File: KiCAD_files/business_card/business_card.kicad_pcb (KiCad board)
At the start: 2 copper layers, 89 x 50.8 mm, 82 parts, among them J1 USB_C_Receptacle_USB2.0_14P, J2 Conn_01x05_Pin, SW1 SW_MEC_5E, SW2 SW_MEC_5E, SW3 SW_MEC_5E, SW4 SW_MEC_5E, SW5 SW_MEC_5E, SW6 SW_MEC_5E, SW7 SW_MEC_5E, SW8 SW_Push, U1 STM32U073CCUx, U2 MCP1700x-300xxTT, U3 TPS3839DBZ

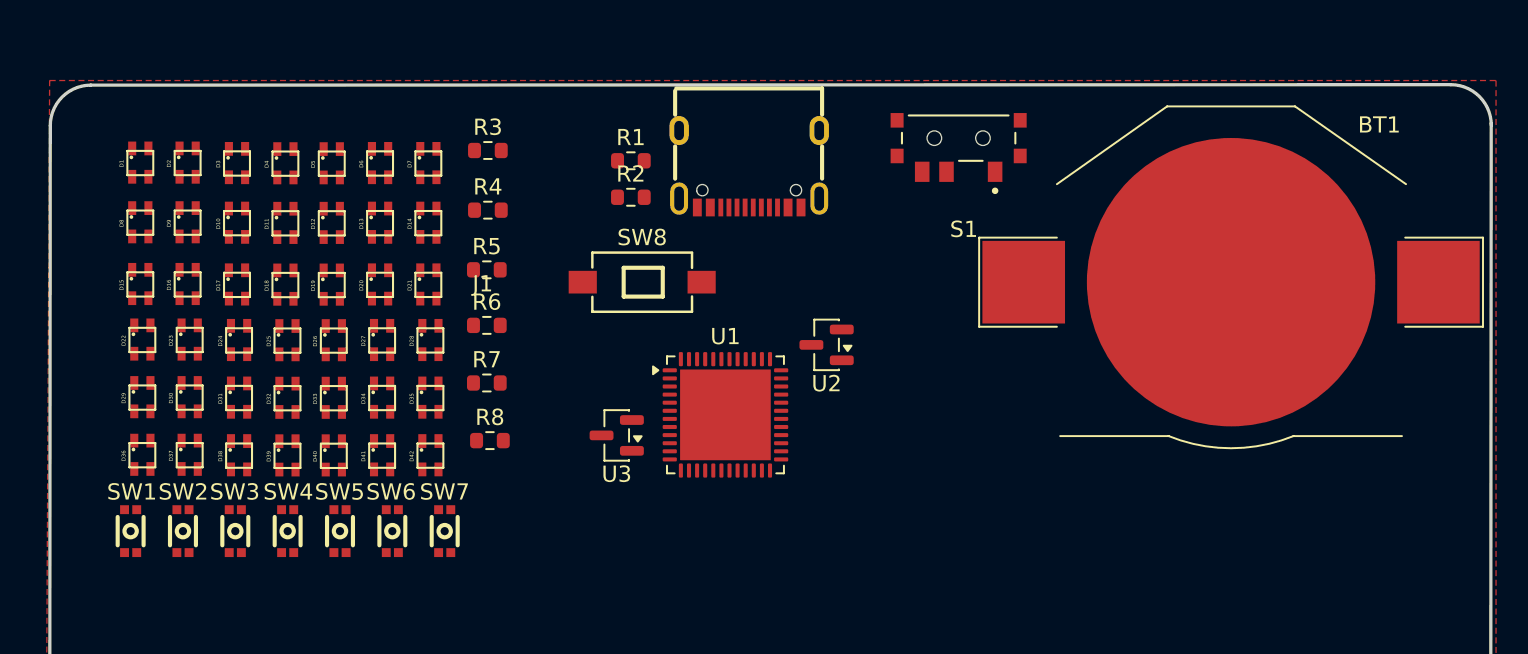
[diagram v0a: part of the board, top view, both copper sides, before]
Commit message: Change Connections to Match STM32C0 Spec
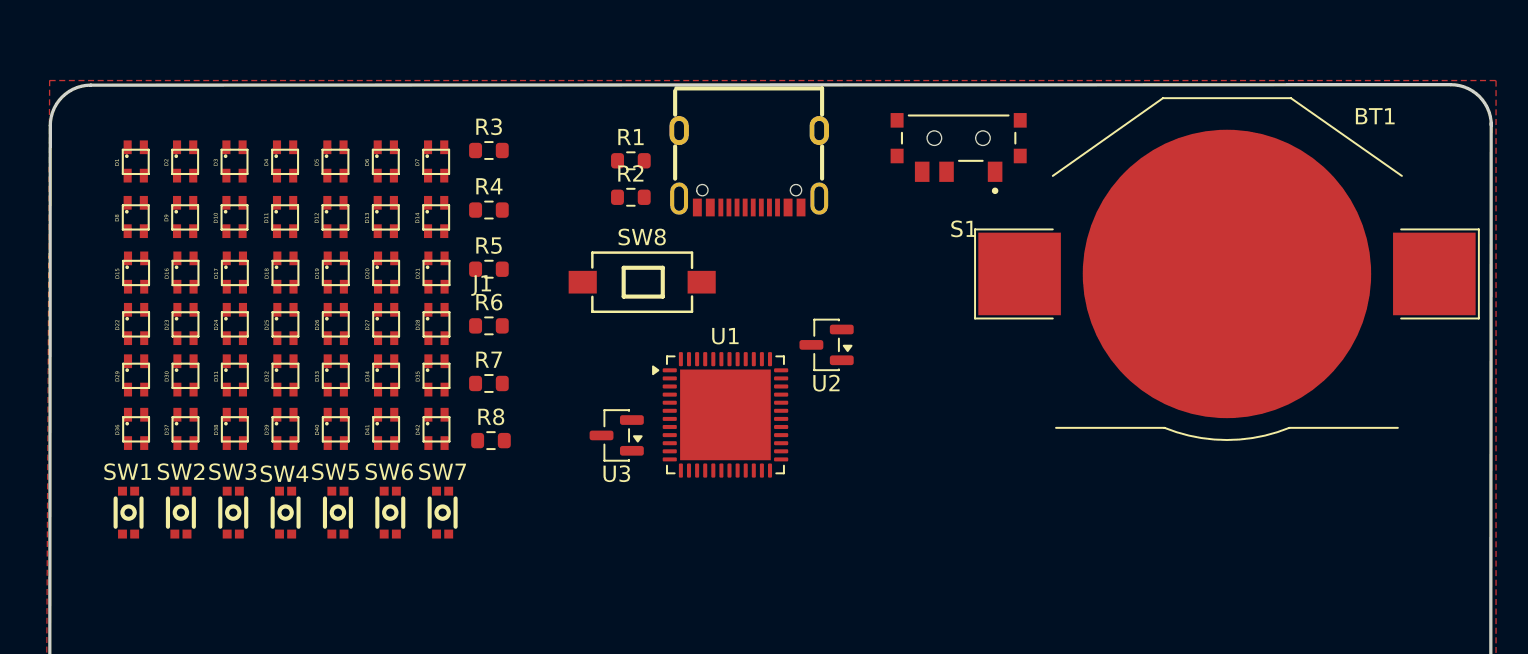
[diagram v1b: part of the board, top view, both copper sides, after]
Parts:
- moved D42 1.67 mm to (113.8, 68.8)
- moved D38 1.64 mm to (101.3, 68.8)
- moved D41 1.64 mm to (110.7, 68.8)
- moved D36 1.64 mm to (95.3, 68.8)
- moved D39 1.64 mm to (104.5, 68.8)
- moved D40 1.64 mm to (107.6, 68.8)
- moved D37 1.62 mm to (98.3, 68.8)
- moved D35 1.42 mm to (113.8, 65.5)
- moved D29 1.40 mm to (95.3, 65.5)
- moved D31 1.39 mm to (101.3, 65.5)
- moved D34 1.39 mm to (110.7, 65.5)
- moved D32 1.39 mm to (104.5, 65.5)
- moved D33 1.39 mm to (107.6, 65.5)
- moved D30 1.37 mm to (98.3, 65.5)
- moved SW2 1.15 mm to (98.0, 74.0)
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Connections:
- S1 pad 1: /VDDUSB -> Net-(BT1-+)
- S1 pad 3: Net-(BT1-+) -> /VDDUSB

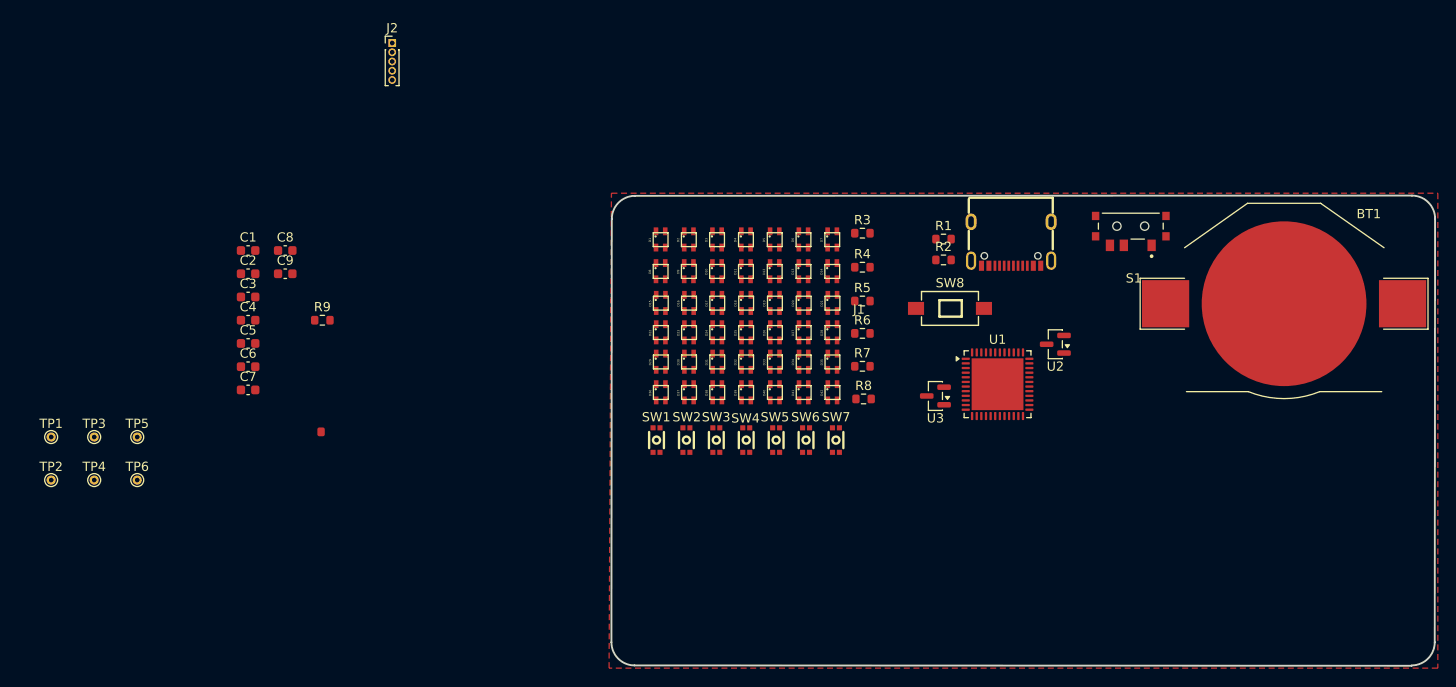
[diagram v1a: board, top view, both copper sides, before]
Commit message: Switch Button types, Add 3D Models to Components
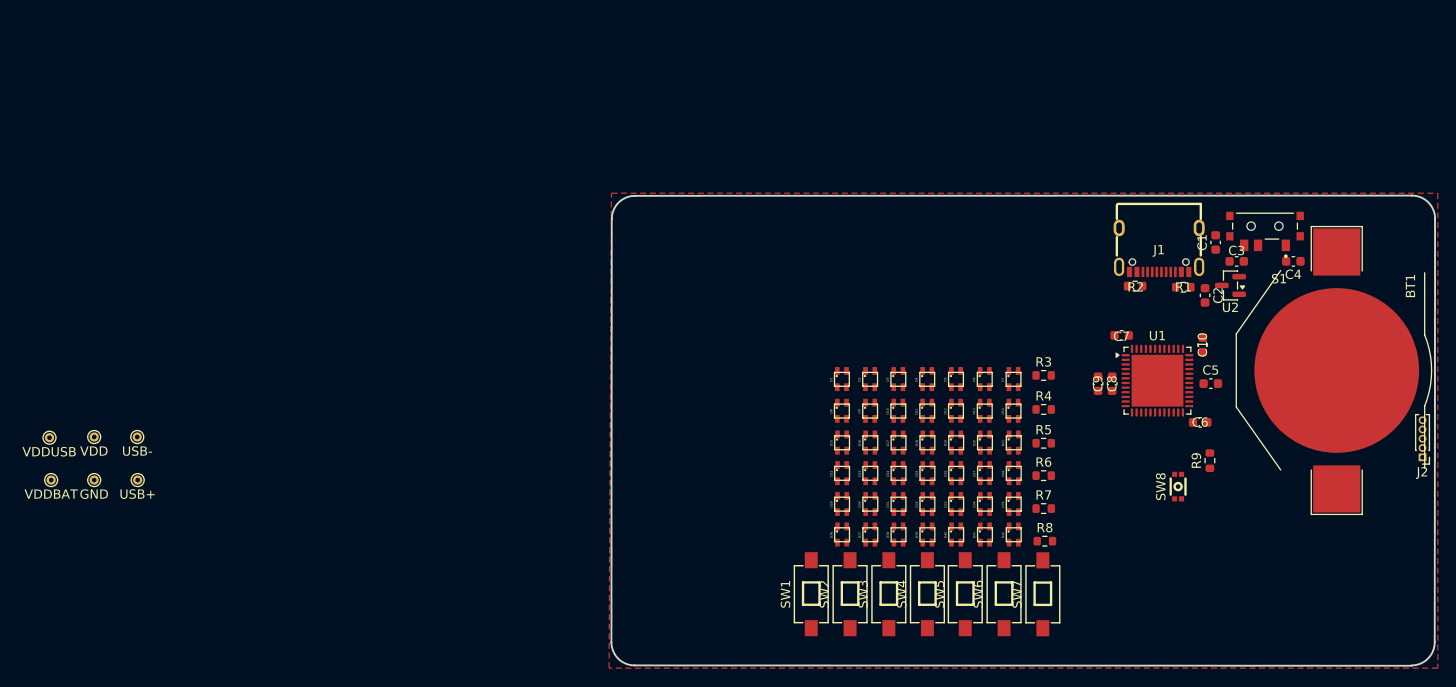
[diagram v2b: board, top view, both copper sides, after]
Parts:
- removed ?: , 
- removed the C4 at (50.7, 61.1)
- removed U3: TPS3839DBZ, Package_TO_SOT_SMD:SOT-23
- added C1: 4.7uF, Capacitor_SMD:C_0603_1608Metric, F.Cu at (155.2, 52.7)
- added C10: 4.7uF, Capacitor_SMD:C_0603_1608Metric, F.Cu at (153.8, 63.8)
- C8: value 1uF -> 10nF
- SW1, SW2, SW3, SW4, SW5, SW6, SW7: value SW_MEC_5E -> SW_Push; footprint 1TS026A-2000-0553-CT:SW-SMD_4P-L2.6-W1.6-P0.75-LS3.0 -> TSB008A2526A:TSB008A2526A
- SW8: value SW_Push -> SW_MEC_5E; footprint TSB008A2526A:TSB008A2526A -> 1TS026A-2000-0553-CT:SW-SMD_4P-L2.6-W1.6-P0.75-LS3.0
- moved J2 120.0 mm to (177.5, 75.9), turned to 180 degrees
- moved C4 108.9 mm to (163.6, 54.7), turned to 180 degrees
- moved C3 107.7 mm to (157.5, 54.7), turned to 180 degrees
- moved C5 105.0 mm to (154.7, 67.9)
- moved C6 104.1 mm to (153.5, 72.1)
- moved C2 103.7 mm to (154.1, 58.4), turned to -90 degrees
- moved R9 97.1 mm to (154.6, 76.3), turned to 90 degrees
- moved C7 94.5 mm to (145.0, 62.7), turned to 180 degrees
- moved C9 91.9 mm to (142.5, 68.0), turned to 90 degrees
- moved C8 90.5 mm to (144.0, 68.0), turned to 90 degrees
- moved SW8 31.3 mm to (151.1, 79.1), turned to 90 degrees
- moved SW7 27.9 mm to (136.5, 90.7)
- moved SW6 27.1 mm to (132.3, 90.7)
- moved R1 26.4 mm to (151.7, 57.5), turned to 180 degrees
- moved SW5 26.4 mm to (128.1, 90.7)
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- renumbered C6 to C2, C7 to C3, C9 to C4, C1 to C5, C2 to C6, C3 to C7, C5 to C9
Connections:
- C5 pad 1: +3.3V -> VDD
- C6 pad 1: +3.3V -> VDD
- C7 pad 1: +3.3V -> VDD
- C8 pad 1: GND -> VDD
- C8 pad 2: +3.3V -> GND
- C9 pad 1: +3.3V -> VDD
- J1 pad 1: (no net) -> GND
- J1 pad 10: (no net) -> Net-(J1-CC2)
- J1 pad 11: (no net) -> Net-(U2-VI)
- J1 pad 12: (no net) -> GND
- J1 pad 13: (no net) -> GND
- J1 pad 14: (no net) -> GND
- J1 pad 2: (no net) -> Net-(U2-VI)
- J1 pad 3: (no net) -> unconnected-(J1-SBU2-Pad3)
- J1 pad 4: (no net) -> Net-(J1-CC1)
- J1 pad 5: (no net) -> /USB-
- J1 pad 6: (no net) -> /USB+
- J1 pad 7: (no net) -> /USB-
- J1 pad 8: (no net) -> /USB+
- J1 pad 9: (no net) -> unconnected-(J1-SBU1-Pad9)
- J2 pad 1: +3.3V -> VDD
- R9 pad 1: Net-(U1-PF3) -> Net-(SW8-A)
- S1 pad 2: +3.3V -> VDD
- SW1 pad 2: unconnected-(SW1-Pad2) -> VDD
- SW2 pad 2: unconnected-(SW2-Pad2) -> VDD
- SW3 pad 2: unconnected-(SW3-Pad2) -> VDD
- SW4 pad 2: unconnected-(SW4-Pad2) -> VDD
- SW5 pad 2: unconnected-(SW5-Pad2) -> VDD
- SW6 pad 2: unconnected-(SW6-Pad2) -> VDD
- SW7 pad 2: unconnected-(SW7-Pad2) -> VDD
- SW8 pad 1: +3.3V -> VDD
- SW8 pad 2: Net-(U1-PF3) -> unconnected-(SW8-Pad2)
- TP3 pad 1: +3.3V -> VDD
- U1 pad 1: +3.3V -> VDD
- U1 pad 10: unconnected-(U1-PA0-Pad10) -> /VDDUSB
- U1 pad 24: +3.3V -> VDD
- U1 pad 36: /VDDUSB -> VDD
- U1 pad 38: /VDDUSB -> unconnected-(U1-PA15-Pad38)
- U1 pad 44: Net-(U1-PF3) -> Net-(SW8-A)
- U1 pad 48: +3.3V -> VDD
- U1 pad 9: GND -> VDD

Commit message: PCB Layout
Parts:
- removed TP4: GND, TestPoint:TestPoint_THTPad_D1.0mm_Drill0.5mm
- removed TP5: USB-, TestPoint:TestPoint_THTPad_D1.0mm_Drill0.5mm
- removed TP6: USB+, TestPoint:TestPoint_THTPad_D1.0mm_Drill0.5mm
- added C11: 100nF, Capacitor_SMD:C_0603_1608Metric, F.Cu at (150.4, 77.5)
- TP2: value VDDBAT -> GND
- moved TP1 141.7 mm to (170.9, 72.1)
- moved TP2 137.5 mm to (166.9, 75.4)
- moved TP3 137.0 mm to (170.9, 70.1)
- moved J2 42.0 mm to (144.8, 49.5), turned to 90 degrees
- moved J1 40.7 mm to (173.0, 86.4), turned to 90 degrees
- moved R1 35.9 mm to (169.0, 89.0), turned to 90 degrees
- moved R2 34.7 mm to (169.1, 83.8), turned to -90 degrees
- moved C1 32.1 mm to (171.7, 80.3), turned to 180 degrees
- moved C7 27.5 mm to (160.0, 85.9), turned to 0 degrees
- moved C2 26.9 mm to (171.7, 78.7), turned to 180 degrees
- moved U2 26.0 mm to (173.7, 77.0), turned to -90 degrees
- moved S1 24.6 mm to (175.3, 70.6), turned to 90 degrees
- moved C3 24.3 mm to (171.4, 74.6), turned to 90 degrees
- moved D15 17.9 mm to (97.0, 74.9), turned to 180 degrees
- moved D1 17.9 mm to (97.0, 68.0), turned to 180 degrees
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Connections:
- D12 pad 1: Net-(D12-Pad1) -> /COL5
- D12 pad 3: Net-(D12-Pad1) -> /COL5
- D13 pad 1: Net-(D13-Pad1) -> /COL6
- D13 pad 3: Net-(D13-Pad1) -> /COL6
- D19 pad 1: Net-(D12-Pad1) -> /COL5
- D19 pad 3: Net-(D12-Pad1) -> /COL5
- D20 pad 1: Net-(D13-Pad1) -> /COL6
- D20 pad 3: Net-(D13-Pad1) -> /COL6
- D26 pad 1: Net-(D12-Pad1) -> /COL5
- D26 pad 3: Net-(D12-Pad1) -> /COL5
- D27 pad 1: Net-(D13-Pad1) -> /COL6
- D27 pad 3: Net-(D13-Pad1) -> /COL6
- D33 pad 1: Net-(D29-Pad2) -> /COL5
- D33 pad 3: Net-(D29-Pad2) -> /COL5
- D34 pad 1: Net-(D13-Pad1) -> /COL6
- D34 pad 3: Net-(D13-Pad1) -> /COL6
- D36 pad 2: /COL5 -> Net-(D36-Pad2)
- D36 pad 4: /COL5 -> Net-(D36-Pad2)
- D37 pad 2: /COL5 -> Net-(D36-Pad2)
- D37 pad 4: /COL5 -> Net-(D36-Pad2)
- D38 pad 2: /COL5 -> Net-(D36-Pad2)
- D38 pad 4: /COL5 -> Net-(D36-Pad2)
- D39 pad 2: /COL5 -> Net-(D36-Pad2)
- D39 pad 4: /COL5 -> Net-(D36-Pad2)
- D40 pad 2: /COL5 -> Net-(D36-Pad2)
- D40 pad 4: /COL5 -> Net-(D36-Pad2)
- D41 pad 1: /COL5 -> /COL6
- D41 pad 2: /COL5 -> Net-(D36-Pad2)
- D41 pad 3: /COL5 -> /COL6
- D41 pad 4: /COL5 -> Net-(D36-Pad2)
- D42 pad 2: /COL5 -> Net-(D36-Pad2)
- D42 pad 4: /COL5 -> Net-(D36-Pad2)
- D5 pad 1: Net-(D12-Pad1) -> /COL5
- D5 pad 3: Net-(D12-Pad1) -> /COL5
- D6 pad 1: Net-(D13-Pad1) -> /COL6
- D6 pad 3: Net-(D13-Pad1) -> /COL6
- R8 pad 1: /COL5 -> Net-(D36-Pad2)
- S1 pad 1: Net-(BT1-+) -> /VDDUSB
- S1 pad 3: /VDDUSB -> Net-(BT1-+)
- TP2 pad 1: Net-(BT1-+) -> GND
- U1 pad 22: /COL5 -> /COL6
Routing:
- net VDD: track 0.00 -> 25.0 mm
- net /COL4: track 0.00 -> 13.9 mm
- net /COL2: track 0.00 -> 13.7 mm
- net /COL5: track 0.00 -> 13.6 mm
- net /COL1: track 0.00 -> 13.5 mm
- net /COL3: track 0.00 -> 13.4 mm
- net /COL6: track 0.00 -> 13.4 mm
- net /COL7: track 0.00 -> 13.3 mm
- net Net-(BT1-+): track 0.00 -> 10.9 mm
- net /USB+: track 0.00 -> 5.38 mm
- net /VDDUSB: track 0.00 -> 4.87 mm
- net /USB-: track 0.00 -> 4.38 mm, vias 0 -> 2
- net Net-(U2-VI): track 0.00 -> 3.11 mm
- net Net-(J1-CC1): track 0.00 -> 1.87 mm
- net Net-(J1-CC2): track 0.00 -> 1.54 mm

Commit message: Fix Edge Cuts
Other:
- board size 89 x 50.8 mm -> 88.9 x 50.8 mm
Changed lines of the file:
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@@
 				(font
 					(size 0.24 0.24)
+					(thickness 0.15)
 				)
 			)
@@
 		(tags "capacitor")
 		(property "Reference" "C10"
-			(at 0 0 90)
+			(at 0 2.292 180)
 			(layer "F.SilkS")
 			(effects
@@
 		)
 	)
-	(gr_arc
-		(start 89.956 50.154767)
-		(mid 90.688245 48.387021)
-		(end 92.456 47.654767)
-		(stroke
-			(width 0.2)
-			(type solid)
-		)
-		(layer "Edge.Cuts")
-	)
 	(gr_line
-		(start 89.956 50.1548)
-		(end 89.916 95.885)
+		(start 176.316 98.298)
+		(end 92.416 98.298)
 		(stroke
-			(width 0.2)
-			(type solid)
+			(width 0.1)
+			(type default)
 		)
 		(layer "Edge.Cuts")
 	)
-	(gr_line
-		(start 176.403 47.625)
-		(end 92.456 47.654767)
+	(gr_arc
+		(start 178.816 95.798)
+		(mid 178.083767 97.565767)
+		(end 176.316 98.298)
 		(stroke
-			(width 0.2)
-			(type solid)
+			(width 0.1)
+			(type default)
 		)
 		(layer "Edge.Cuts")
 	)
 	(gr_arc
-		(start 92.416 98.385)
-		(mid 90.648233 97.652767)
-		(end 89.916 95.885)
+		(start 89.916 49.998)
+		(mid 90.648233 48.230233)
+		(end 92.416 47.498)
 		(stroke
-			(width 0.2)
-			(type solid)
+			(width 0.1)
+			(type default)
 		)
 		(layer "Edge.Cuts")
 	)
 	(gr_line
-		(start 92.416 98.385)
-		(end 176.363 98.425)
+		(start 89.916 95.798)
+		(end 89.916 49.998)
 		(stroke
-			(width 0.2)
-			(type solid)
+			(width 0.1)
+			(type default)
 		)
 		(layer "Edge.Cuts")
 	)
 	(gr_arc
-		(start 178.863 95.885)
-		(mid 178.130767 97.652767)
-		(end 176.363 98.385)
+		(start 176.316 47.498)
+		(mid 178.083767 48.230233)
+		(end 178.816 49.998)
 		(stroke
-			(width 0.2)
-			(type solid)
+			(width 0.1)
+			(type default)
 		)
 		(layer "Edge.Cuts")
 	)
 	(gr_line
-		(start 178.863 95.885)
-		(end 178.9 50.002563)
+		(start 92.416 47.498)
+		(end 176.316 47.498)
 		(stroke
-			(width 0.2)
-			(type solid)
+			(width 0.1)
+			(type default)
+		)
+		(layer "Edge.Cuts")
+	)
+	(gr_line
+		(start 178.816 49.998)
+		(end 178.816 95.798)
+		(stroke
+			(width 0.1)
+			(type default)
 		)
 		(layer "Edge.Cuts")
 	)
 	(gr_arc
-		(start 176.403 47.625)
-		(mid 178.170767 48.357233)
-		(end 178.903 50.125)
+		(start 92.416 98.298)
+		(mid 90.648233 97.565767)
+		(end 89.916 95.798)
 		(stroke
-			(width 0.2)
-			(type solid)
+			(width 0.1)
+			(type default)
 		)
 		(layer "Edge.Cuts")
@@
 		(min_thickness 0.25)
 		(filled_areas_thickness no)
-		(fill yes
+		(fill
 			(thermal_gap 0.5)
 			(thermal_bridge_width 0.5)
@@
 		(polygon
 			(pts
-				(xy 89.916 47.371) (xy 179.197 47.371) (xy 179.197 98.679) (xy 89.662 98.679)
+				(xy 89.789 47.371) (xy 179.07 47.371) (xy 179.07 98.425) (xy 89.535 98.425)
 			)
 		)
